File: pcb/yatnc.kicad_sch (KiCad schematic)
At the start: 24 parts, among them J1 Conn_01x10_Socket, J3 Conn_01x02_Socket, J4 Conn_01x03_Pin, J5 Conn_02x02_Top_Bottom, J6 Conn_01x13_Socket, J7 Conn_01x13_Socket, Q1 BC547, SW1 SW_Push, U1 MAX3232

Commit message: Fix DRC errors
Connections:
- net GND: now also R2.2; no longer R1.1
- net VCC: now also R1.1; no longer R2.2

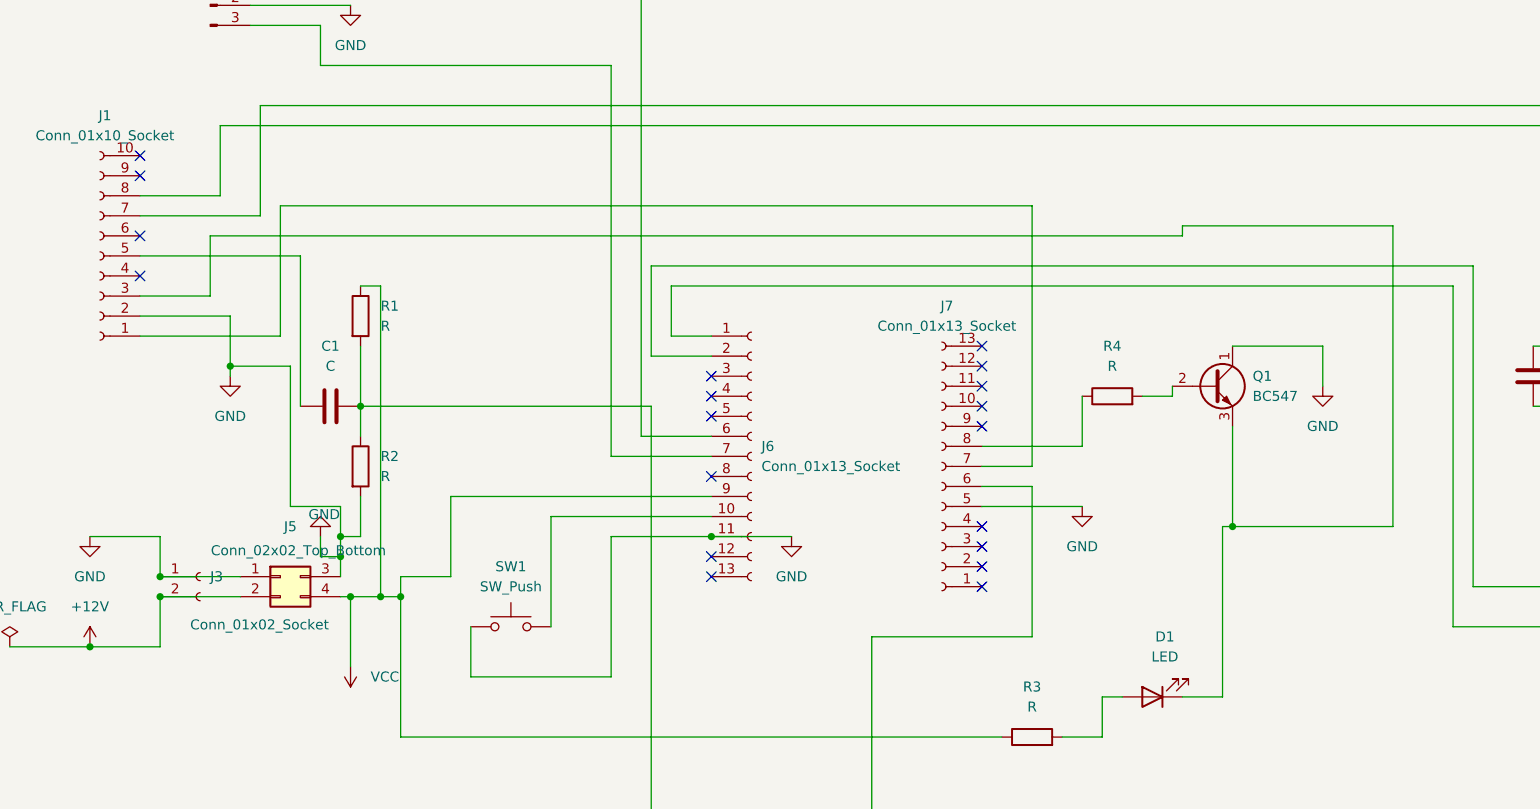
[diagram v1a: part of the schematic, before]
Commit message: add into schema 2 stage RC filter
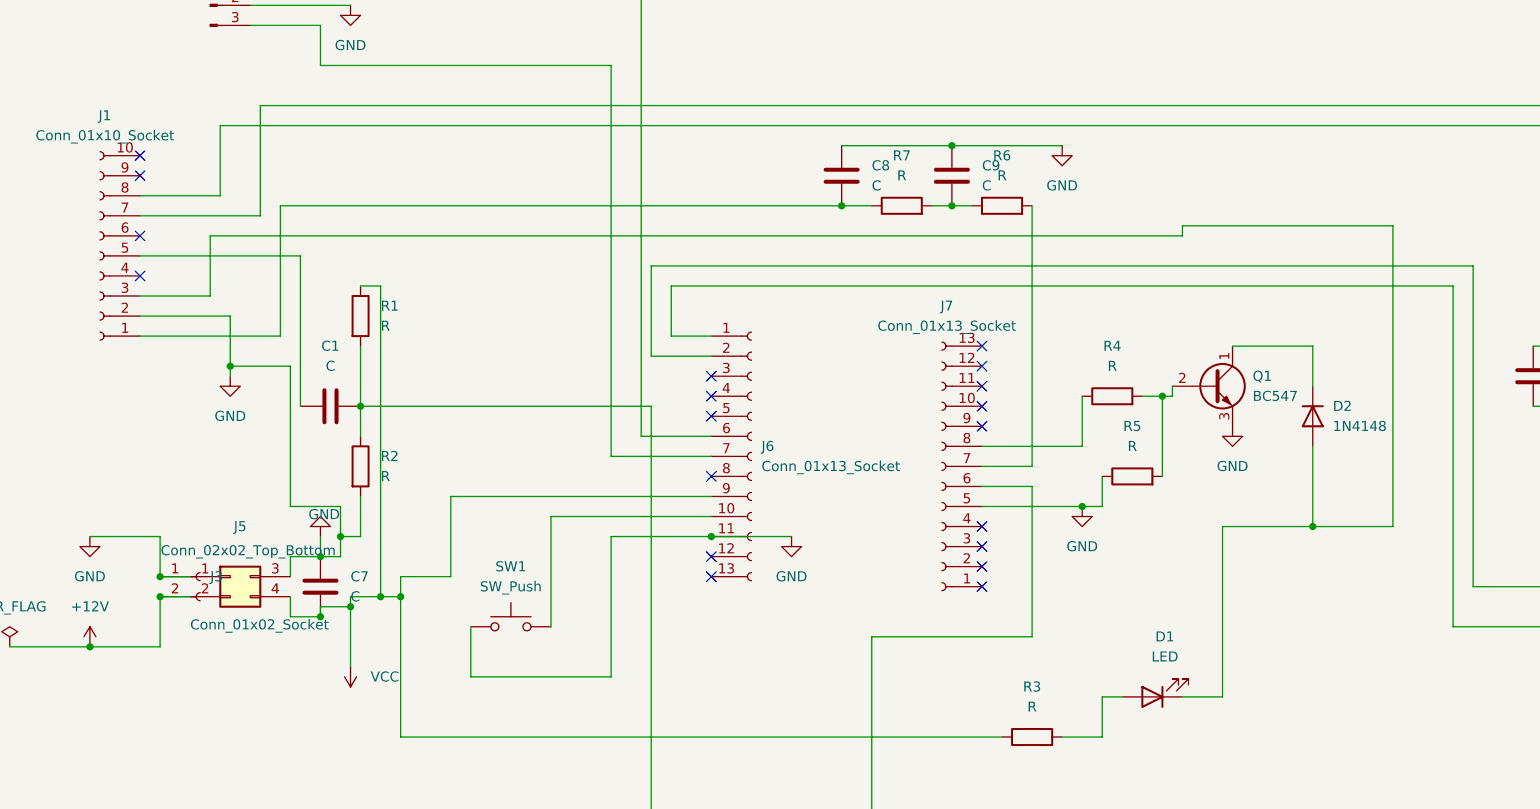
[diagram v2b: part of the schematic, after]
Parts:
- added C7, C8, C9: C, Capacitor_THT:C_Disc_D5.0mm_W2.5mm_P5.00mm, symbol Device:C
- added D2: 1N4148, Diode_THT:D_DO-35_SOD27_P7.62mm_Horizontal, symbol Diode:1N4148
- added R5, R6, R7: R, Resistor_THT:R_Axial_DIN0207_L6.3mm_D2.5mm_P10.16mm_Horizontal, symbol Device:R
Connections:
- net GND: now also Q1.3 (E), C7.2, C8.1, C9.1, R5.1; no longer Q1.1 (C)
- net VCC: now also C7.1
- net at J7.7 (Pin_7): now also R6.2; no longer J1.1 (Pin_1)
- net at D1.1 (K), J1.3 (Pin_3): now also D2.2 (A); no longer Q1.3 (E)
- net at Q1.2 (B), R4.2: now also R5.2
- new net: D2.1 (K), Q1.1 (C)
- new net: C8.2, J1.1 (Pin_1), R7.1
- new net: C9.2, R6.1, R7.2
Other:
- moved on the sheet: J5

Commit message: added afsk filter and vin protection
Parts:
- added C10: C_Polarized, Capacitor_THT:CP_Radial_D8.0mm_P5.00mm, symbol Device:C_Polarized
- added C11: C, Capacitor_THT:C_Disc_D5.0mm_W2.5mm_P5.00mm, symbol Device:C
- added D3: 1N5822, Diode_THT:D_DO-201AD_P15.24mm_Horizontal, symbol Diode:1N5822
- added D4: PTVS18VZ1USK, Diode_THT:D_DO-15_P10.16mm_Horizontal, symbol Diode:PTVS18VZ1USK
- added L1: L, Inductor_THT:L_Radial_D7.0mm_P3.00mm, symbol Device:L
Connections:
- net GND: now also C10.2, C11.1, D4.2 (A)
- net VCC: now also D3.2 (A)
- net +12V: no longer names the net of J3.2 (Pin_2), J5.2 (Pin_2)
- net +12V: now also C10.1, C11.2, D4.1 (K), L1.2
- new net: D3.1 (K), L1.1
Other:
- moved on the sheet: J3, J5

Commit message: resolve ERC/DRC. add cleaning silkscreen, add component values
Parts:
- C1, C11, C2, C3, C4, C5, C6, C7: value C -> 100nF
- C10: value C_Polarized -> 470µF
- C8, C9: value C -> 4.7 nF
- D4: value PTVS18VZ1USK -> BZW04
- J5: value Conn_02x02_Top_Bottom -> DFR0570
- L1: value L -> 47µH
- R1, R2, R3, R5: value R -> 10k
- R4, R6, R7: value R -> 1k
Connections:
- net GND: now also J3.2 (Pin_2); no longer J3.1 (Pin_1)
- net VCC: no longer D3.2 (A)
- net at C10.1, C11.2, D4.1 (K)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: no longer J3.2 (Pin_2)
- new net: D3.2 (A), J3.1 (Pin_1)
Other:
- moved on the sheet: D3, J3, J5, L1

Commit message: first part of changes after review
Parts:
- removed L1: 47µH, Inductor_THT:L_Radial_D7.0mm_P3.00mm, symbol Device:L
- added R8: 1ohm, Resistor_THT:R_Axial_DIN0207_L6.3mm_D2.5mm_P10.16mm_Horizontal, symbol Device:R
- D4: value BZW04 -> BZW04 18V
- J1: value Conn_01x10_Socket -> JST
- SW1: value SW_Push -> RST
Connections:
- net GND: now also U1.8 (R2IN)
- net AUDIO OUT: now reaches J7.7 (Pin_7), R6.2
- net PTT: now reaches D1.1 (K), D2.2 (A), J1.3 (Pin_3)
- net PKD: now reaches C8.2, J1.1 (Pin_1), R7.1
- net AUDIO IN: now reaches C1.1, J1.5 (Pin_5)
- net RX: now reaches J1.7 (Pin_7)
- net RX: now also U1.13 (R1IN); no longer U1.8 (R2IN)
- net TX: now reaches J1.8 (Pin_8), U1.7 (T2OUT)
- net TX: now also U1.14 (T1OUT)
- net TNC: now reaches J4.1 (Pin_1), J6.6 (Pin_6)
- net DIGI: now reaches J4.3 (Pin_3), J6.7 (Pin_7)
- net at C10.1, C11.2, D4.1 (K)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: now also R8.2
- net at J6.2 (Pin_2), U1.10 (T2IN): now also U1.11 (T1IN)
- net at D3.1 (K): now also R8.1
- net VCC renamed 3.3V
- no-connect marks 23 -> 20
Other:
- note added: "Bell 202 low-pass filter"
- note added: "Bias & filter"
- note added: "JST to mini din 10 PIN"
- note added: "Operation mode selector"
- note added: "Power supply & protection"
- moved on the sheet: C1, C10, C11, C2, C3, C4, C5, C6, C7, C8, C9, D1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

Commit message: second part of changes after review
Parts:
- removed C7: 100nF, Capacitor_THT:C_Disc_D5.0mm_W2.5mm_P5.00mm, symbol Device:C
- added C4: 100nF, Capacitor_THT:C_Disc_D5.0mm_W2.5mm_P5.00mm, symbol Device:C
- added C6: 470µF, Capacitor_THT:CP_Radial_D8.0mm_P5.00mm, symbol Device:C_Polarized
- added D1: LED, LED_THT:LED_D5.0mm, symbol Device:LED
- added R1: 10k, Resistor_THT:R_Axial_DIN0207_L6.3mm_D2.5mm_P10.16mm_Horizontal, symbol Device:R
- Q1: footprint Package_TO_SOT_THT:TO-92_Inline -> Package_TO_SOT_THT:TO-92_Inline_Wide
- renumbered C10 to C1, C4 to C10, C5 to C11, C6 to C12, C11 to C2, C8 to C3, C9 to C5, C1 to C7, C2 to C8, C3 to C9, D3 to D2, D4 to D3, D1 to D4, D2 to D5, H2 to H1, H1 to H2, J4 to J1, J1 to J2, J5 to J4, J6 to J5, J7 to J6, R8 to R2, R7 to R3, R6 to R4, R4 to R5, R5 to R6, R3 to R7, R2 to R8, R1 to R9
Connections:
- net 3.3V: now also C4.2, C6.1, R1.1
- net GND: now also C4.1, C6.2, D1.1 (K)
- new net: D1.2 (A), R1.2
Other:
- note added: "Power indicator"
- moved on the sheet: C7, R8, R9

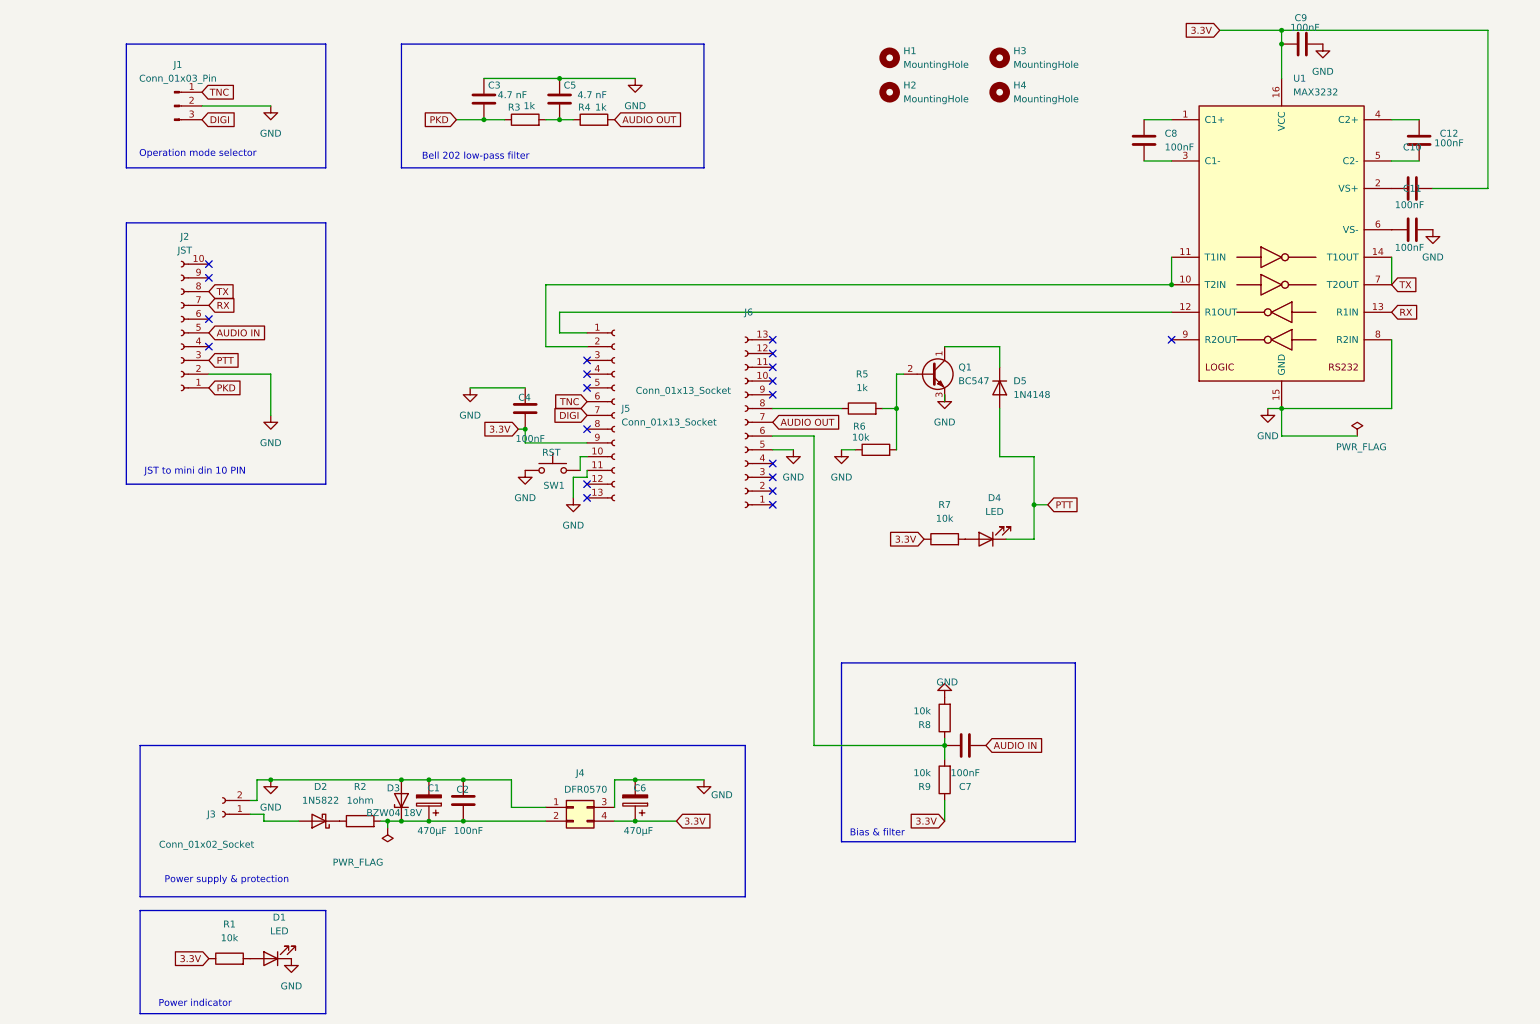
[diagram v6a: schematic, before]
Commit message: added GPS
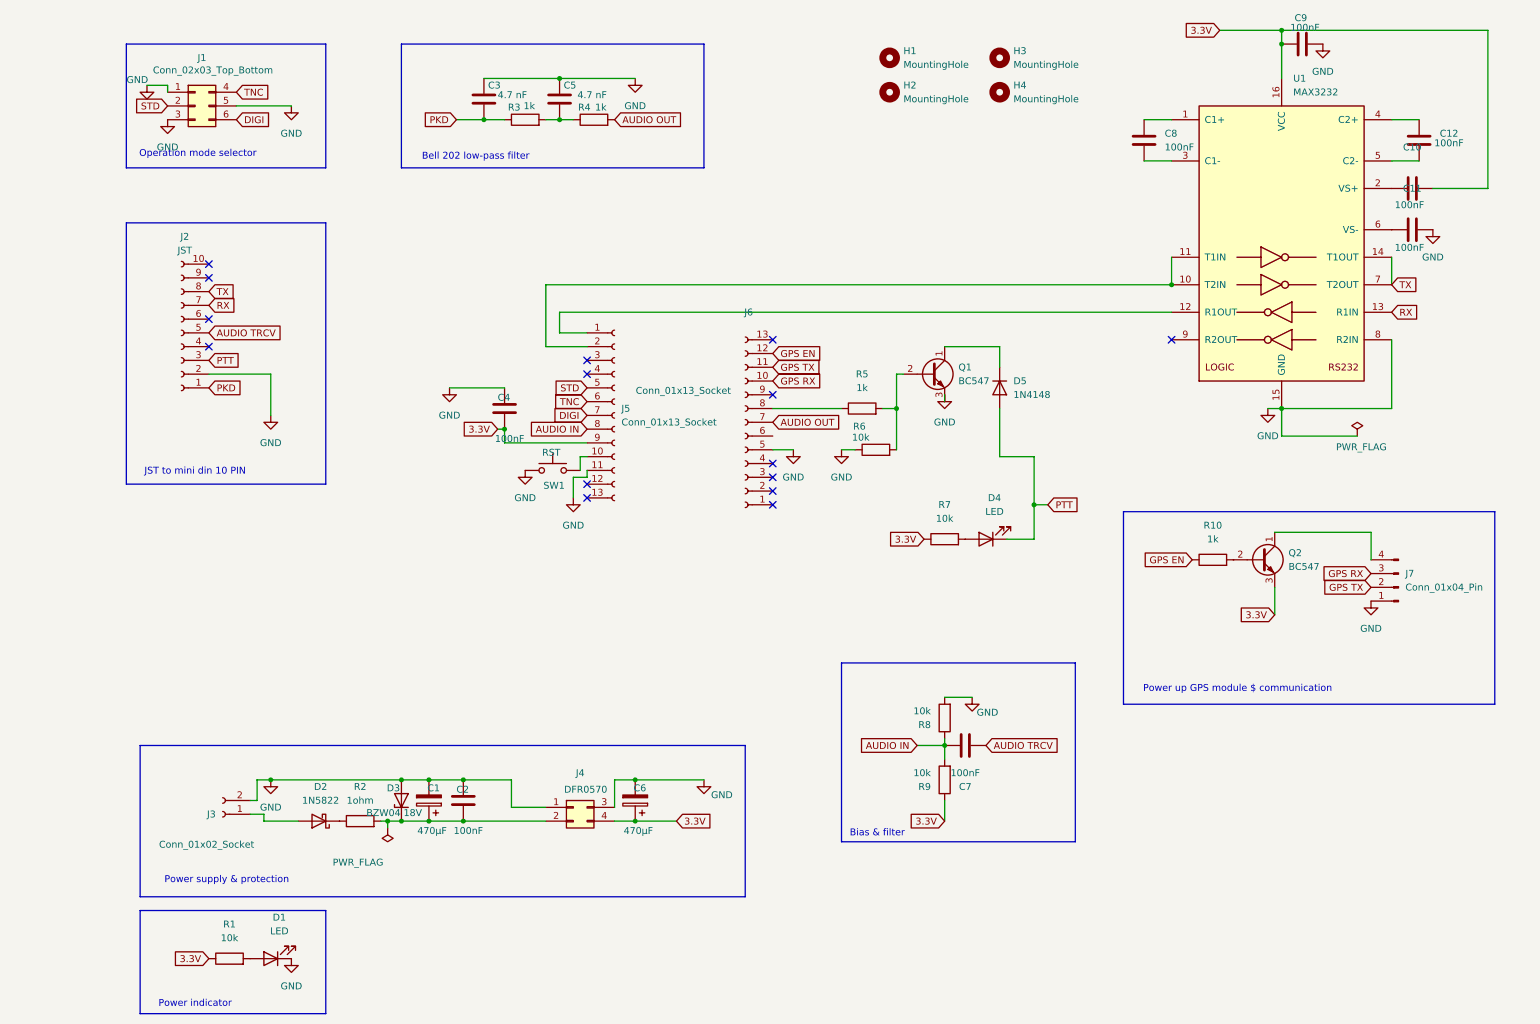
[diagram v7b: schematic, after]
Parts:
- removed J1: Conn_01x03_Pin, Connector_PinHeader_2.54mm:PinHeader_1x03_P2.54mm_Vertical, symbol Connector:Conn_01x03_Pin
- added J1: Conn_02x03_Top_Bottom, Connector_PinHeader_2.54mm:PinHeader_2x03_P2.54mm_Vertical, symbol Connector_Generic:Conn_02x03_Top_Bottom
- added J7: Conn_01x04_Pin, Connector_JST:JST_EH_B4B-EH-A_1x04_P2.50mm_Vertical, symbol Connector:Conn_01x04_Pin
- added Q2: BC547, Package_TO_SOT_THT:TO-92_Inline_Wide, symbol Transistor_BJT:BC547
- added R10: 1k, Resistor_THT:R_Axial_DIN0207_L6.3mm_D2.5mm_P10.16mm_Horizontal, symbol Device:R
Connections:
- net 3.3V: now also Q2.3 (E)
- net AUDIO IN: now also C7.2, J5.8 (Pin_8), R8.1, R9.2; no longer C7.1, J2.5 (Pin_5)
- net DIGI: now also J1.6 (Pin_6)
- net GND: now also J1.1 (Pin_1), J1.3 (Pin_3), J1.5 (Pin_5), J7.1 (Pin_1)
- net TNC: now also J1.4 (Pin_4)
- net GPS RX: now reaches J6.10 (Pin_10)
- net GPS RX: now also J7.3 (Pin_3)
- net GPS TX: now reaches J6.11 (Pin_11)
- net GPS TX: now also J7.2 (Pin_2)
- net GPS EN: now reaches J6.12 (Pin_12)
- net GPS EN: now also R10.1
- net STD: now reaches J5.5 (Pin_5)
- net STD: now also J1.2 (Pin_2)
- new net: J7.4 (Pin_4), Q2.1 (C)
- new net: Q2.2 (B), R10.2
- new net AUDIO TRCV: C7.1, J2.5 (Pin_5)
- now unconnected: J6.6 (Pin_6)
- no-connect marks 20 -> 15
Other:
- note added: "Power up GPS module $ communication"
- moved on the sheet: C4

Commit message: max3232 refactor
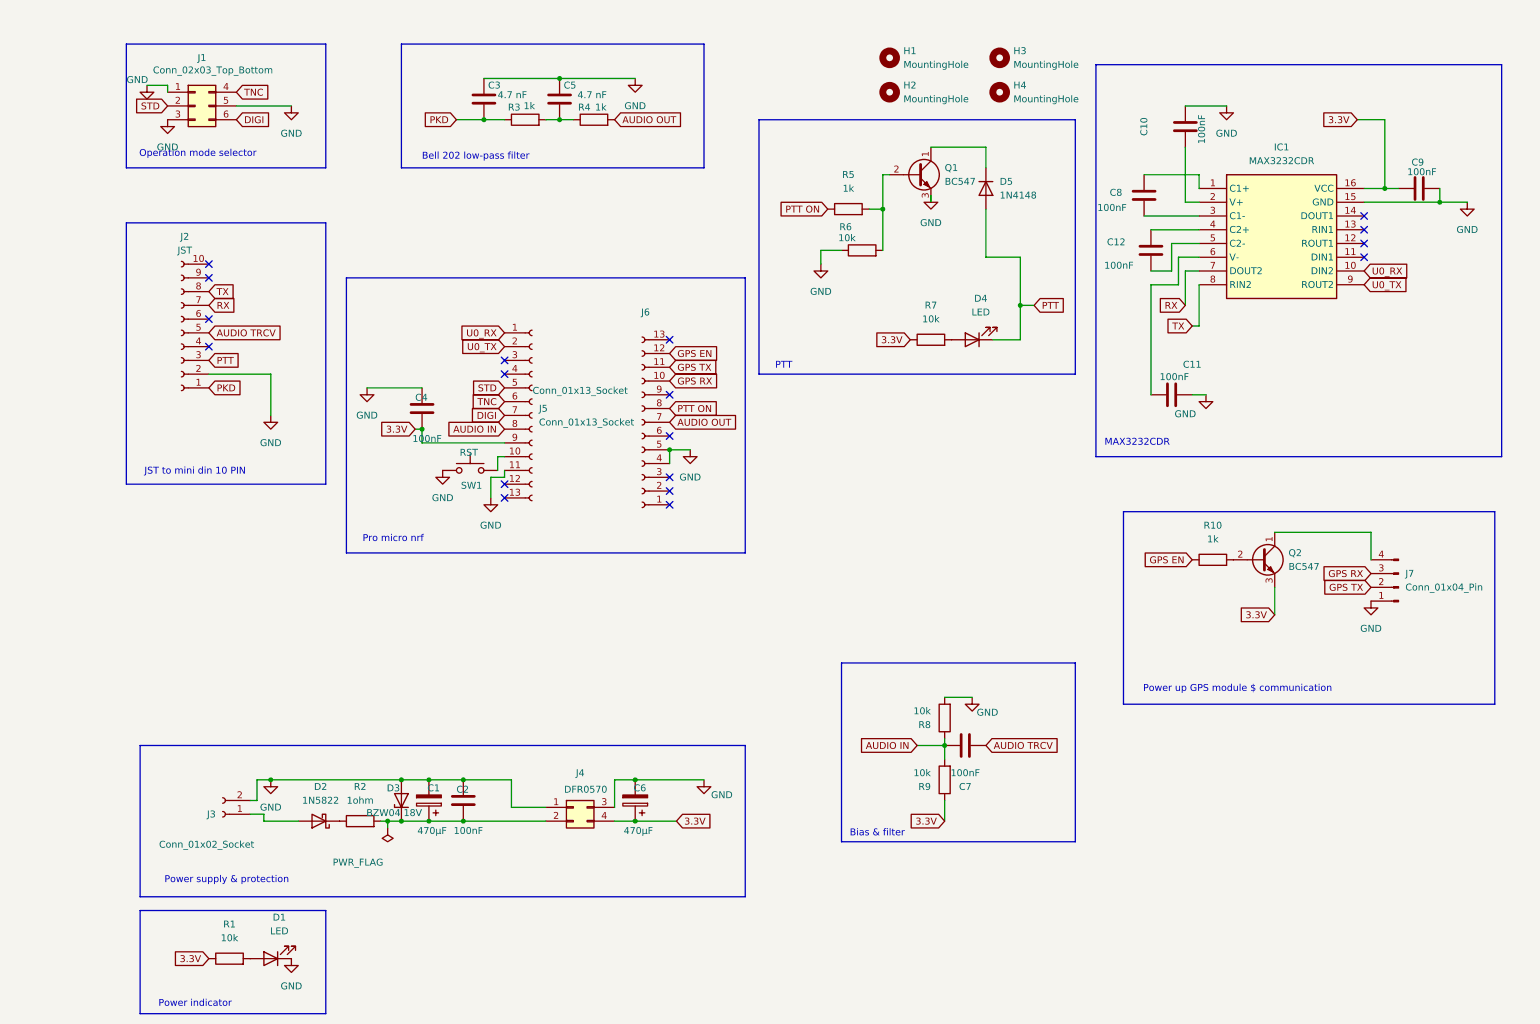
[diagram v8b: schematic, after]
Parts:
- removed U1: MAX3232, liby:SOIC127P600X175-16N, symbol Interface_UART:MAX3232
- added IC1: MAX3232CDR, liby:SOIC127P600X175-16N, symbol MAX3232CDR:MAX3232CDR
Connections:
- net 3.3V: now also IC1.16 (VCC); no longer C10.2
- net GND: now also C10.2, C11.1, J6.4 (Pin_4), IC1.15 (GND); no longer C11.2
- net RX: now also IC1.7 (DOUT2)
- net TX: now also IC1.8 (RIN2)
- net PTT ON: now reaches J6.8 (Pin_8), R5.1
- net at C12.1: now also IC1.4 (C2+)
- net at C12.2: now also IC1.5 (C2-)
- net at C8.1: now also IC1.1 (C1+)
- net at C8.2: now also IC1.3 (C1-)
- net at C10.1: now also IC1.2 (V+)
- net U0_TX: now reaches J5.2 (Pin_2)
- net U0_TX: now also IC1.9 (ROUT2)
- net U0_RX: now reaches J5.1 (Pin_1)
- net U0_RX: now also IC1.10 (DIN2)
- new net: C11.2, IC1.6 (V-)
- no-connect marks 15 -> 18
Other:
- note added: "MAX3232CDR"
- note added: "PTT"
- note added: "Pro micro nrf"
- moved on the sheet: C10, C11, C12, C4, C8, C9, D4, D5, J5, J6, Q1, R5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
